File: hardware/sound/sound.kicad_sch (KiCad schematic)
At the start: 38 parts, among them J1 Conn_01x02, J2 AVR-ISP-6, J3 Conn_01x02, J4 Conn_01x02, J5 Conn_01x02, J6 Conn_01x04, T1 125BSE, U1 6CY7, U2 SN76489, U3 ATtiny84A-P, X1 CXO_DIP8

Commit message: working on placement
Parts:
- added C10, C9: 0.1uF, Capacitor_THT:C_Disc_D3.4mm_W2.1mm_P2.50mm, symbol Device:C
- added C11: 2.2uF, Capacitor_THT:C_Disc_D3.4mm_W2.1mm_P2.50mm, symbol Device:C
- C3: value C -> 33uF 400V
- C8: value C -> 0.1uF
- LS1: footprint Connector_PinHeader_2.54mm:PinHeader_1x02_P2.54mm_Vertical -> Connector_Phoenix_MC_HighVoltage:PhoenixContact_MCV_1,5_2-G-5.08_1x02_P5.08mm_Vertical; CatNo 36-4109-ND -> 277-12547-ND
- R10: footprint Resistor_SMD:R_1206_3216Metric_Pad1.30x1.75mm_HandSolder -> Resistor_THT:R_Axial_DIN0204_L3.6mm_D1.6mm_P5.08mm_Horizontal
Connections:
- net +5V: now also C10.2, C11.2, C9.2
- net Earth: now also C10.1, C11.1, C9.1
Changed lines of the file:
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@@
   (junction (at 64.135 74.93) (diameter 0) (color 0 0 0 0)
   )
+  (junction (at 90.17 48.26) (diameter 0) (color 0 0 0 0)
+  )
   (junction (at 187.96 143.51) (diameter 0) (color 0 0 0 0)
   )
@@
     (stroke (width 0) (type default))
   )
-  (wire (pts (xy 90.17 47.625) (xy 90.17 52.07))
+  (wire (pts (xy 81.28 48.26) (xy 90.17 48.26))
+    (stroke (width 0) (type default))
+  )
+  (wire (pts (xy 90.17 47.625) (xy 90.17 48.26))
     (stroke (width 0) (type default))
   )
@@
     (stroke (width 0) (type default))
   )
+  (wire (pts (xy 67.31 52.07) (xy 67.31 48.26))
+    (stroke (width 0) (type default))
+  )
   (wire (pts (xy 231.775 52.705) (xy 236.22 52.705))
     (stroke (width 0) (type default))
@@
     (stroke (width 0) (type default))
   )
+  (wire (pts (xy 67.31 48.26) (xy 73.66 48.26))
+    (stroke (width 0) (type default))
+  )
   (wire (pts (xy 175.26 151.13) (xy 214.63 151.13))
     (stroke (width 0) (type default))
@@
     (stroke (width 0) (type default))
   )
+  (wire (pts (xy 90.17 48.26) (xy 90.17 52.07))
+    (stroke (width 0) (type default))
+  )
   (wire (pts (xy 34.925 125.73) (xy 34.925 129.54))
     (stroke (width 0) (type default))
@@
     (stroke (width 0) (type default))
   )
-  (text "PSG" (at 78.105 52.07 0)
+  (text "PSG" (at 86.36 38.1 0)
     (effects (font (size 1.905 1.905)) (justify left bottom))
   )
@@
       (effects (font (size 1.27 1.27)))
     )
-    (property "Value" "C" (at 109.22 70.485 90)
+    (property "Value" "0.1uF" (at 109.22 70.485 90)
       (effects (font (size 1.27 1.27)))
     )
@@
       (effects (font (size 1.27 1.27)))
     )
-    (property "Footprint" "Resistor_SMD:R_1206_3216Metric_Pad1.30x1.75mm_HandSolder" (at 80.899 103.124 90)
+    (property "Footprint" "Resistor_THT:R_Axial_DIN0204_L3.6mm_D1.6mm_P5.08mm_Horizontal" (at 80.899 103.124 90)
       (effects (font (size 1.27 1.27)) hide)
     )
@@
     )
   )
+  (symbol (lib_id "Device:C") (at 62.23 152.4 0) (mirror x) (unit 1)
+    (in_bom yes) (on_board yes) (dnp no)
+    (property "Reference" "C11" (at 67.31 156.21 90)
+      (effects (font (size 1.27 1.27)))
+    )
+    (property "Value" "2.2uF" (at 67.31 149.86 90)
+      (effects (font (size 1.27 1.27)))
+    )
+    (property "Footprint" "Capacitor_THT:C_Disc_D3.4mm_W2.1mm_P2.50mm" (at 63.1952 148.59 0)
+      (effects (font (size 1.27 1.27)) hide)
+    )
+    (property "Datasheet" "~" (at 62.23 152.4 0)
+      (effects (font (size 1.27 1.27)) hide)
+    )
+    (pin "2")
+    (pin "1")
+    (instances
+      (project "sound"
+        (path "/43f7f6bf-f4bb-437b-bd97-246f0a609f68"
+          (reference "C11") (unit 1)
+        )
+      )
+    )
+  )
   (symbol (lib_id "power:Earth") (at 139.7 46.99 0) (unit 1)
     (in_bom yes) (on_board yes) (dnp no)
@@
         (path "/43f7f6bf-f4bb-437b-bd97-246f0a609f68"
           (reference "#PWR01") (unit 1)
+        )
+      )
+    )
+  )
+  (symbol (lib_id "power:Earth") (at 67.31 52.07 0) (unit 1)
+    (in_bom yes) (on_board yes) (dnp no)
+    (property "Reference" "#PWR023" (at 67.31 58.42 0)
+      (effects (font (size 1.27 1.27)) hide)
+    )
+    (property "Value" "Earth" (at 67.31 55.88 0)
+      (effects (font (size 1.27 1.27)) hide)
+    )
+    (property "Footprint" "" (at 67.31 52.07 0)
+      (effects (font (size 1.27 1.27)) hide)
+    )
+    (property "Datasheet" "~" (at 67.31 52.07 0)
+      (effects (font (size 1.27 1.27)) hide)
+    )
+    (pin "1")
+    (instances
+      (project "sound"
+        (path "/43f7f6bf-f4bb-437b-bd97-246f0a609f68"
+          (reference "#PWR023") (unit 1)
         )
       )
@@
     )
   )
+  (symbol (lib_id "Device:C") (at 22.86 49.53 0) (mirror x) (unit 1)
+    (in_bom yes) (on_board yes) (dnp no)
+    (property "Reference" "C10" (at 27.94 53.34 90)
+      (effects (font (size 1.27 1.27)))
+    )
+    (property "Value" "0.1uF" (at 27.94 46.99 90)
+      (effects (font (size 1.27 1.27)))
+    )
+    (property "Footprint" "Capacitor_THT:C_Disc_D3.4mm_W2.1mm_P2.50mm" (at 23.8252 45.72 0)
+      (effects (font (size 1.27 1.27)) hide)
+    )
+    (property "Datasheet" "~" (at 22.86 49.53 0)
+      (effects (font (size 1.27 1.27)) hide)
+    )
+    (pin "2")
+    (pin "1")
+    (instances
+      (project "sound"
+        (path "/43f7f6bf-f4bb-437b-bd97-246f0a609f68"
+          (reference "C10") (unit 1)
+        )
+      )
+    )
+  )
   (symbol (lib_id "power:+5V") (at 34.925 125.73 0) (unit 1)
     (in_bom yes) (on_board yes) (dnp no) (fields_autoplaced)
@@
   (symbol (lib_id "Device:C") (at 139.7 43.18 0) (unit 1)
     (in_bom yes) (on_board yes) (dnp no) (fields_autoplaced)
-    (property "Reference" "C3" (at 142.875 41.91 0)
-      (effects (font (size 1.27 1.27)) (justify left))
-    )
-    (property "Value" "C" (at 142.875 44.45 0)
+    (property "Reference" "C3" (at 143.51 41.91 0)
+      (effects (font (size 1.27 1.27)) (justify left))
+    )
+    (property "Value" "33uF 400V" (at 143.51 44.45 0)
       (effects (font (size 1.27 1.27)) (justify left))
     )
@@
         (path "/43f7f6bf-f4bb-437b-bd97-246f0a609f68"
           (reference "#PWR012") (unit 1)
+        )
+      )
+    )
+  )
+  (symbol (lib_id "power:Earth") (at 22.86 53.34 0) (unit 1)
+    (in_bom yes) (on_board yes) (dnp no)
+    (property "Reference" "#PWR025" (at 22.86 59.69 0)
+      (effects (font (size 1.27 1.27)) hide)
+    )
+    (property "Value" "Earth" (at 22.86 57.15 0)
+      (effects (font (size 1.27 1.27)) hide)
+    )
+    (property "Footprint" "" (at 22.86 53.34 0)
+      (effects (font (size 1.27 1.27)) hide)
+    )
+    (property "Datasheet" "~" (at 22.86 53.34 0)
+      (effects (font (size 1.27 1.27)) hide)
+    )
+    (pin "1")
+    (instances
+      (project "sound"
+        (path "/43f7f6bf-f4bb-437b-bd97-246f0a609f68"
+          (reference "#PWR025") (unit 1)
         )
       )
@@
     )
   )
+  (symbol (lib_id "power:+5V") (at 22.86 45.72 0) (unit 1)
+    (in_bom yes) (on_board yes) (dnp no) (fields_autoplaced)
+    (property "Reference" "#PWR024" (at 22.86 49.53 0)
+      (effects (font (size 1.27 1.27)) hide)
+    )
+    (property "Value" "+5V" (at 22.86 40.64 0)
+      (effects (font (size 1.27 1.27)))
+    )
+    (property "Footprint" "" (at 22.86 45.72 0)
+      (effects (font (size 1.27 1.27)) hide)
+    )
+    (property "Datasheet" "" (at 22.86 45.72 0)
+      (effects (font (size 1.27 1.27)) hide)
+    )
+    (pin "1")
+    (instances
+      (project "sound"
+        (path "/43f7f6bf-f4bb-437b-bd97-246f0a609f68"
+          (reference "#PWR024") (unit 1)
+        )
+      )
+    )
+  )
   (symbol (lib_id "Mechanical:MountingHole") (at 33.655 170.815 0) (unit 1)
     (in_bom yes) (on_board yes) (dnp no) (fields_autoplaced)
@@
       (effects (font (size 1.27 1.27)) (justify left))
     )
-    (property "Footprint" "Connector_PinHeader_2.54mm:PinHeader_1x02_P2.54mm_Vertical" (at 241.3 48.26 0)
+    (property "Footprint" "Connector_Phoenix_MC_HighVoltage:PhoenixContact_MCV_1,5_2-G-5.08_1x02_P5.08mm_Vertical" (at 241.3 48.26 0)
       (effects (font (size 1.27 1.27)) hide)
     )
@@
       (effects (font (size 1.27 1.27)) hide)
     )
-    (property "CatNo" "36-4109-ND" (at 245.618 46.7614 0)
+    (property "CatNo" "277-12547-ND" (at 245.618 46.7614 0)
       (effects (font (size 1.27 1.27)) (justify left))
     )
@@
         (path "/43f7f6bf-f4bb-437b-bd97-246f0a609f68"
           (reference "U1") (unit 2)
+        )
+      )
+    )
+  )
+  (symbol (lib_id "Device:C") (at 77.47 48.26 90) (mirror x) (unit 1)
+    (in_bom yes) (on_board yes) (dnp no)
+    (property "Reference" "C9" (at 73.66 53.34 90)
+      (effects (font (size 1.27 1.27)))
+    )
+    (property "Value" "0.1uF" (at 80.01 53.34 90)
+      (effects (font (size 1.27 1.27)))
+    )
+    (property "Footprint" "Capacitor_THT:C_Disc_D3.4mm_W2.1mm_P2.50mm" (at 81.28 49.2252 0)
+      (effects (font (size 1.27 1.27)) hide)
+    )
+    (property "Datasheet" "~" (at 77.47 48.26 0)
+      (effects (font (size 1.27 1.27)) hide)
+    )
+    (pin "2")
+    (pin "1")
+    (instances
+      (project "sound"
+        (path "/43f7f6bf-f4bb-437b-bd97-246f0a609f68"
+          (reference "C9") (unit 1)
         )
       )
@@
     )
   )
+  (symbol (lib_id "power:+5V") (at 62.23 148.59 0) (unit 1)
+    (in_bom yes) (on_board yes) (dnp no) (fields_autoplaced)
+    (property "Reference" "#PWR026" (at 62.23 152.4 0)
+      (effects (font (size 1.27 1.27)) hide)
+    )
+    (property "Value" "+5V" (at 62.23 143.51 0)
+      (effects (font (size 1.27 1.27)))
+    )
+    (property "Footprint" "" (at 62.23 148.59 0)
+      (effects (font (size 1.27 1.27)) hide)
+    )
+    (property "Datasheet" "" (at 62.23 148.59 0)
+      (effects (font (size 1.27 1.27)) hide)
+    )
+    (pin "1")
+    (instances
+      (project "sound"
+        (path "/43f7f6bf-f4bb-437b-bd97-246f0a609f68"
+          (reference "#PWR026") (unit 1)
+        )
+      )
+    )
+  )
   (symbol (lib_id "power:+5V") (at 55.88 30.48 0) (unit 1)
     (in_bom yes) (on_board yes) (dnp no) (fields_autoplaced)
@@
         )
       )
+    )
+  )
+  (symbol (lib_id "power:Earth") (at 62.23 156.21 0) (unit 1)
+    (in_bom yes) (on_board yes) (dnp no)
+    (property "Reference" "#PWR027" (at 62.23 162.56 0)
+      (effects (font (size 1.27 1.27)) hide)
+    )
+    (property "Value" "Earth" (at 62.23 160.02 0)
+      (effects (font (size 1.27 1.27)) hide)
+    )
+    (property "Footprint" "" (at 62.23 156.21 0)
+      (effects (font (size 1.27 1.27)) hide)
+    )
+    (property "Datasheet" "~" (at 62.23 156.21 0)
+      (effects (font (size 1.27 1.27)) hide)
+    )
+    (pin "1")
+    (instances
+      (project "sound"
+        (path "/43f7f6bf-f4bb-437b-bd97-246f0a609f68"
+          (reference "#PWR027") (unit 1)
+        )
+      )

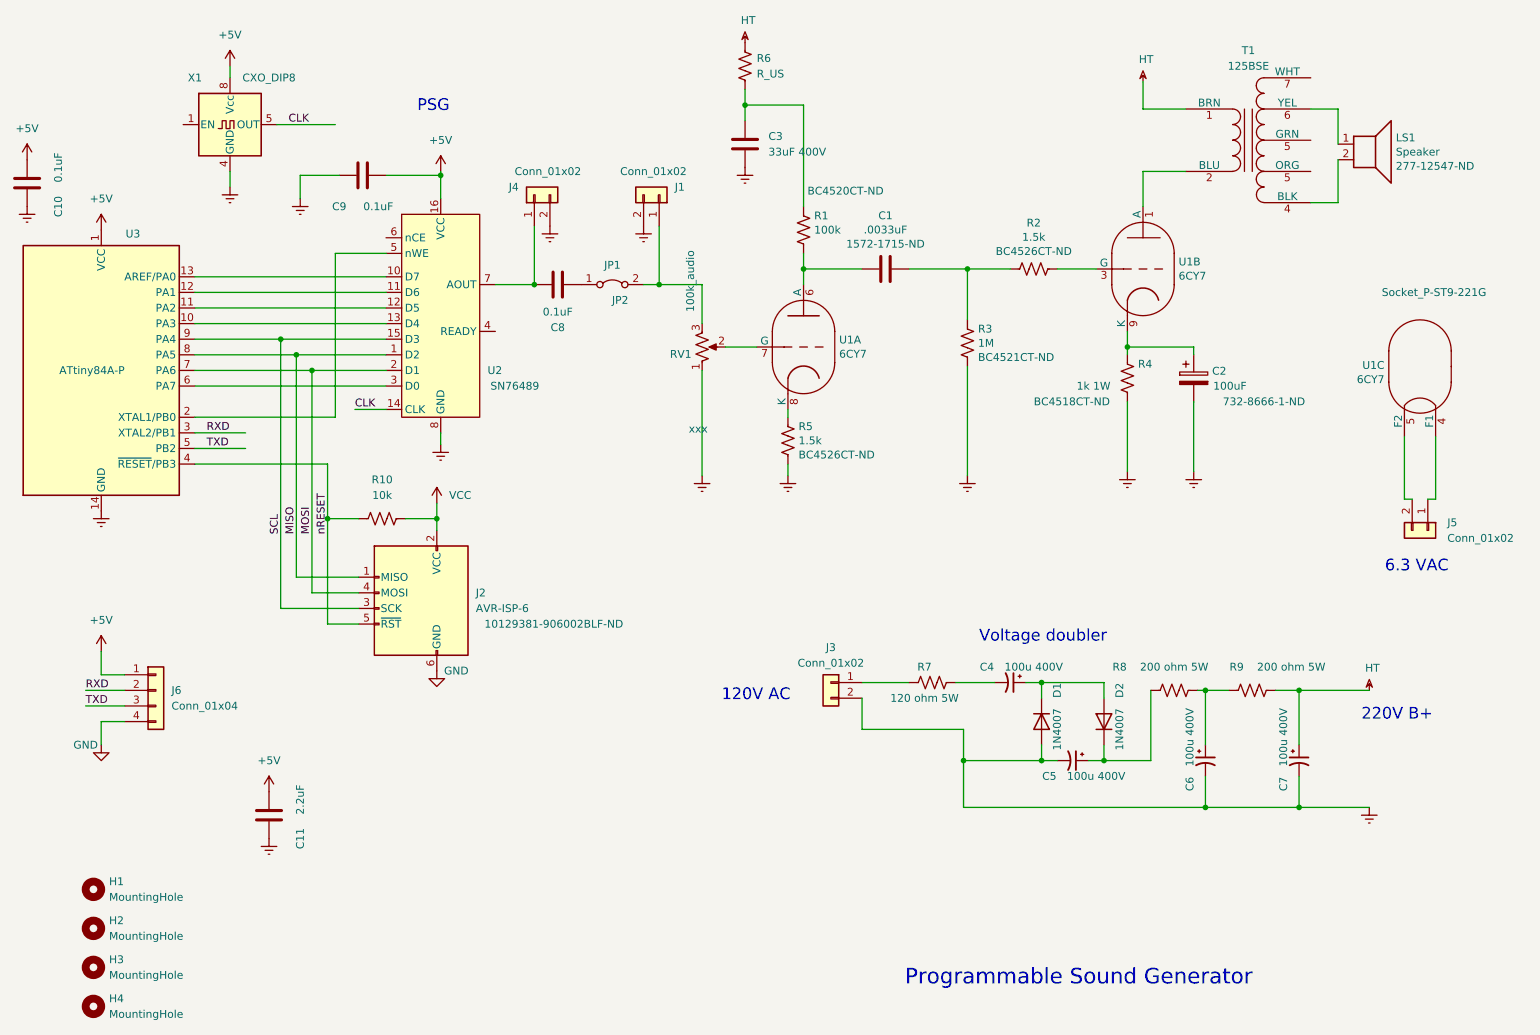
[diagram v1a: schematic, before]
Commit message: work on placement, HV clearance
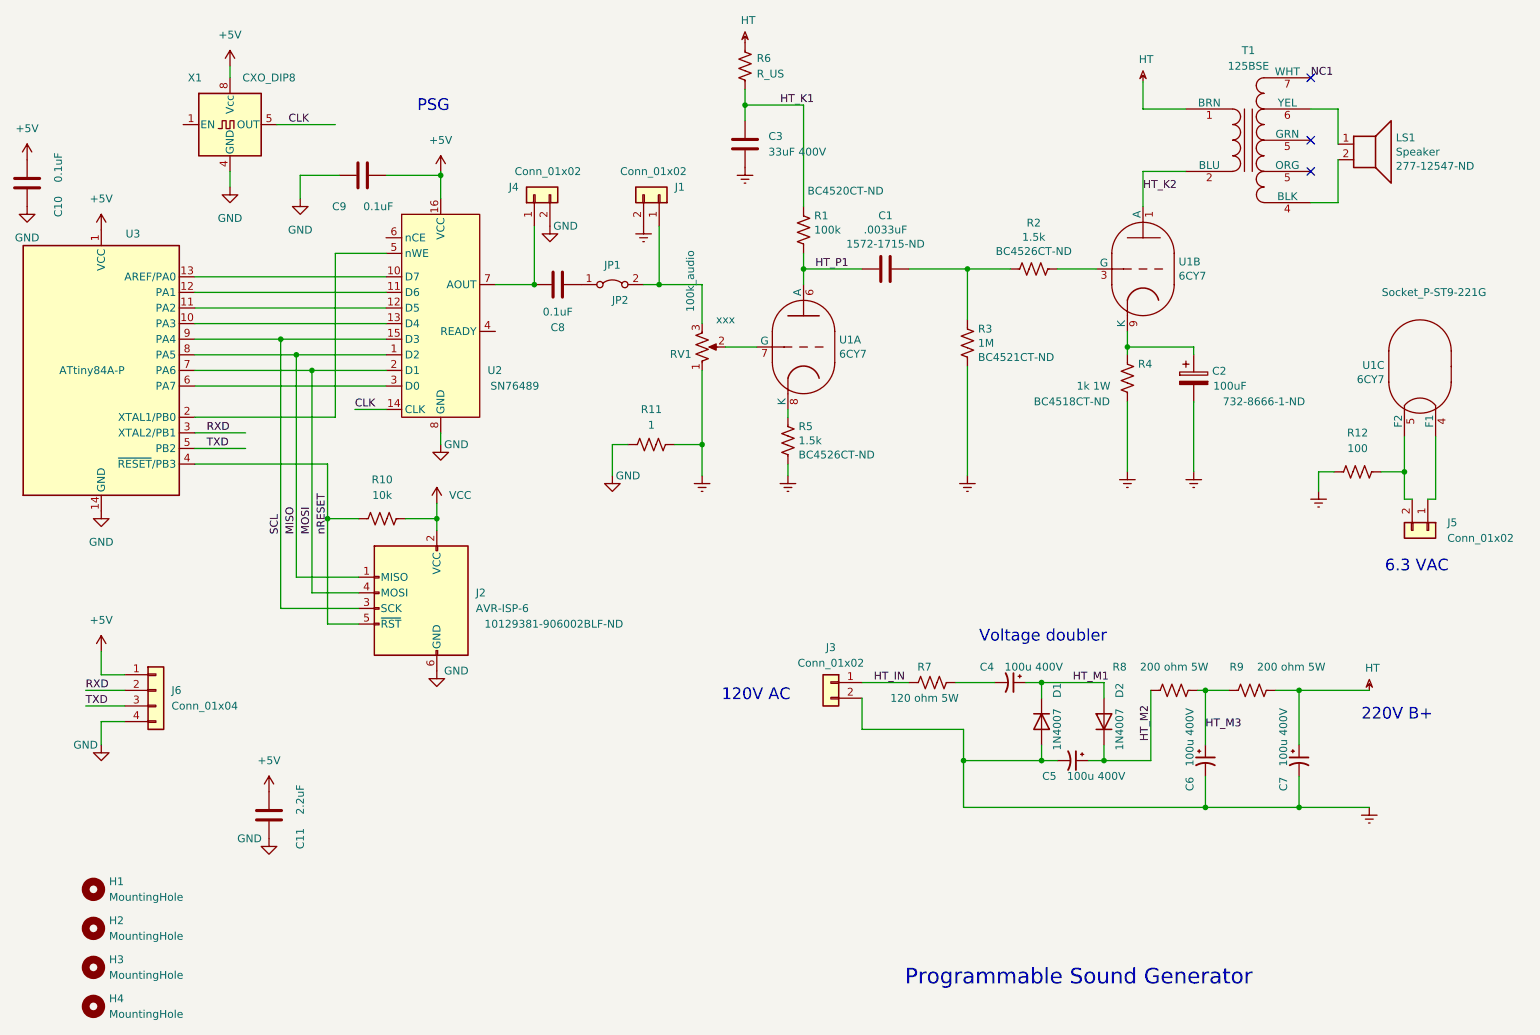
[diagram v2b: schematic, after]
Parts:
- added R11: 1, Resistor_THT:R_Axial_DIN0204_L3.6mm_D1.6mm_P5.08mm_Horizontal, symbol Device:R_US
- added R12: 100, Resistor_THT:R_Axial_DIN0204_L3.6mm_D1.6mm_P5.08mm_Horizontal, symbol Device:R_US
- J6: footprint Connector_PinHeader_2.54mm:PinHeader_1x04_P2.54mm_Horizontal -> Connector_PinHeader_2.54mm:PinHeader_1x04_P2.54mm_Vertical
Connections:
- net Earth: now also R11.2, R12.1; no longer C10.1, C11.1, C9.1, J4.2 (Pin_2), U2.8 (GND), U3.14 (GND), X1.4 (GND)
- net GND: now also C10.1, C11.1, C9.1, J4.2 (Pin_2), U2.8 (GND), U3.14 (GND), X1.4 (GND), R11.1
- net HT_IN: now reaches J3.1 (Pin_1), R7.1
- net HT_K1: now reaches C3.1, R1.1, R6.2
- net HT_P1: now reaches C1.2, R1.2, U1.6 (A)
- net HT_M1: now reaches C4.1, D1.1 (K), D2.2 (A)
- net at J5.2 (Pin_2), U1.5 (F2): now also R12.2
- net HT_M2: now reaches C5.1, D2.1 (K), R8.1
- net HT_M3: now reaches C6.1, R8.2, R9.1
- net HT_K2: now reaches T1.2 (BLU), U1.1 (A)
- net NC1: now reaches T1.7 (WHT)
- no-connect marks 0 -> 3

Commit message: working on placement
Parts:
- added F1: Fuse, symbol Device:Fuse
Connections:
- net HT_IN: now also F1.1; no longer R7.1
- new net HT_FUSE: F1.2, R7.1
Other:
- moved on the sheet: J3
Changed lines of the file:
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@@
     (stroke (width 0) (type default))
   )
-  (wire (pts (xy 158.75 130.81) (xy 166.37 130.81))
+  (wire (pts (xy 136.525 130.81) (xy 147.32 130.81))
     (stroke (width 0) (type default))
   )
@@
     (stroke (width 0) (type default))
   )
+  (wire (pts (xy 154.94 130.81) (xy 166.37 130.81))
+    (stroke (width 0) (type default))
+  )
   (wire (pts (xy 81.28 74.93) (xy 64.135 74.93))
     (stroke (width 0) (type default))
@@
     (stroke (width 0) (type default))
   )
-  (wire (pts (xy 158.75 133.35) (xy 158.75 138.43))
+  (wire (pts (xy 136.525 133.35) (xy 136.525 138.43))
     (stroke (width 0) (type default))
   )
@@
     (stroke (width 0) (type default))
   )
-  (wire (pts (xy 158.75 138.43) (xy 175.26 138.43))
+  (wire (pts (xy 136.525 138.43) (xy 175.26 138.43))
     (stroke (width 0) (type default))
   )
@@
     (effects (font (size 1.905 1.905)) (justify left bottom))
   )
-  (text "120V AC" (at 135.89 133.985 0)
+  (text "120V AC" (at 114.935 133.35 0)
     (effects (font (size 1.905 1.905)) (justify left bottom))
   )
@@
     (effects (font (size 1.27 1.27)) (justify left bottom))
   )
-  (label "HT_IN" (at 160.655 130.81 0) (fields_autoplaced)
+  (label "HT_IN" (at 137.795 130.81 0) (fields_autoplaced)
     (effects (font (size 1.27 1.27)) (justify left bottom))
   )
@@
   )
   (label "NC1" (at 231.775 32.385 0) (fields_autoplaced)
+    (effects (font (size 1.27 1.27)) (justify left bottom))
+  )
+  (label "HT_FUSE" (at 156.21 130.81 0) (fields_autoplaced)
     (effects (font (size 1.27 1.27)) (justify left bottom))
   )
@@
         (path "/43f7f6bf-f4bb-437b-bd97-246f0a609f68"
           (reference "#PWR07") (unit 1)
+        )
+      )
+    )
+  )
+  (symbol (lib_id "Device:Fuse") (at 151.13 130.81 90) (unit 1)
+    (in_bom yes) (on_board yes) (dnp no) (fields_autoplaced)
+    (property "Reference" "F1" (at 151.13 125.095 90)
+      (effects (font (size 1.27 1.27)))
+    )
+    (property "Value" "Fuse" (at 151.13 127.635 90)
+      (effects (font (size 1.27 1.27)))
+    )
+    (property "Footprint" "" (at 151.13 132.588 90)
+      (effects (font (size 1.27 1.27)) hide)
+    )
+    (property "Datasheet" "~" (at 151.13 130.81 0)
+      (effects (font (size 1.27 1.27)) hide)
+    )
+    (pin "2")
+    (pin "1")
+    (instances
+      (project "sound"
+        (path "/43f7f6bf-f4bb-437b-bd97-246f0a609f68"
+          (reference "F1") (unit 1)
         )
       )
@@
     )
   )
-  (symbol (lib_id "Connector_Generic:Conn_01x02") (at 153.67 130.81 0) (mirror y) (unit 1)
+  (symbol (lib_id "Connector_Generic:Conn_01x02") (at 131.445 130.81 0) (mirror y) (unit 1)
     (in_bom yes) (on_board yes) (dnp no) (fields_autoplaced)
-    (property "Reference" "J3" (at 153.67 125.095 0)
-      (effects (font (size 1.27 1.27)))
-    )
-    (property "Value" "Conn_01x02" (at 153.67 127.635 0)
-      (effects (font (size 1.27 1.27)))
-    )
-    (property "Footprint" "Connector_TE-Connectivity:TE_826576-2_1x02_P3.96mm_Vertical" (at 153.67 130.81 0)
-      (effects (font (size 1.27 1.27)) hide)
-    )
-    (property "Datasheet" "~" (at 153.67 130.81 0)
-      (effects (font (size 1.27 1.27)) hide)
-    )
+    (property "Reference" "J3" (at 131.445 125.095 0)
+      (effects (font (size 1.27 1.27)))
+    )
+    (property "Value" "Conn_01x02" (at 131.445 127.635 0)
+      (effects (font (size 1.27 1.27)))
+    )
+    (property "Footprint" "Connector_TE-Connectivity:TE_826576-2_1x02_P3.96mm_Vertical" (at 131.445 130.81 0)
+      (effects (font (size 1.27 1.27)) hide)
+    )
+    (property "Datasheet" "~" (at 131.445 130.81 0)
+      (effects (font (size 1.27 1.27)) hide)
+    )
